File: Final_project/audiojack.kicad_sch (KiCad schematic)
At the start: 15 parts

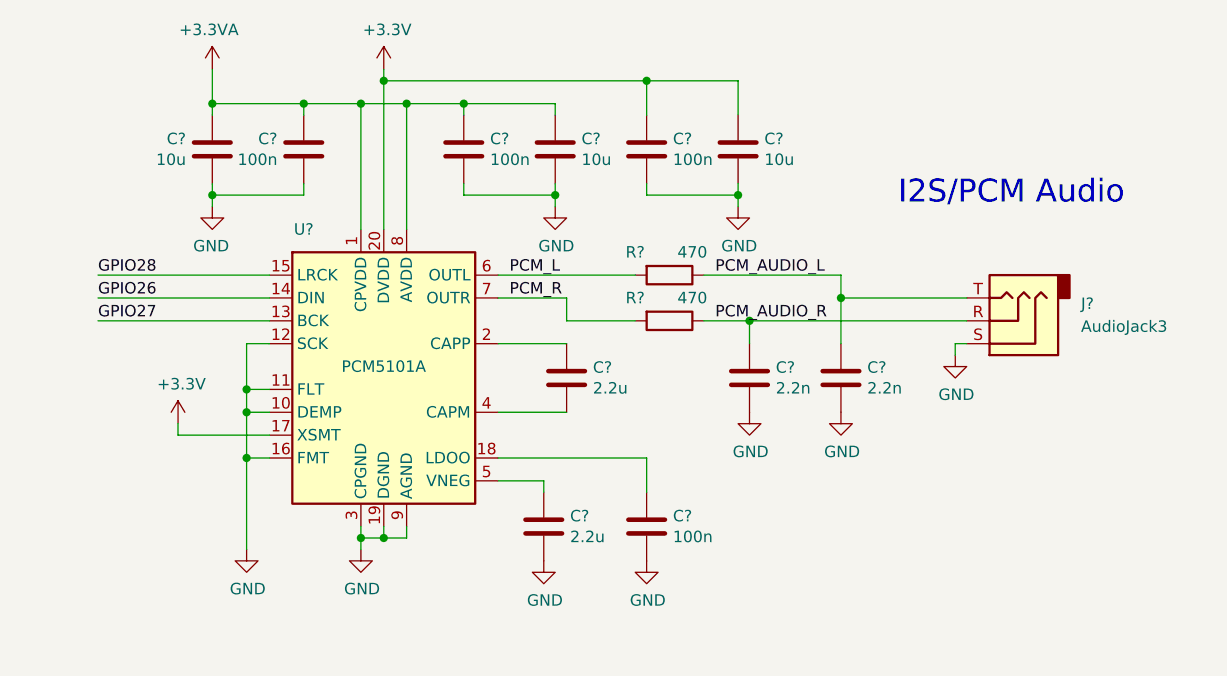
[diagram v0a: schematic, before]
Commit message: assigned footprints to audiojack caps
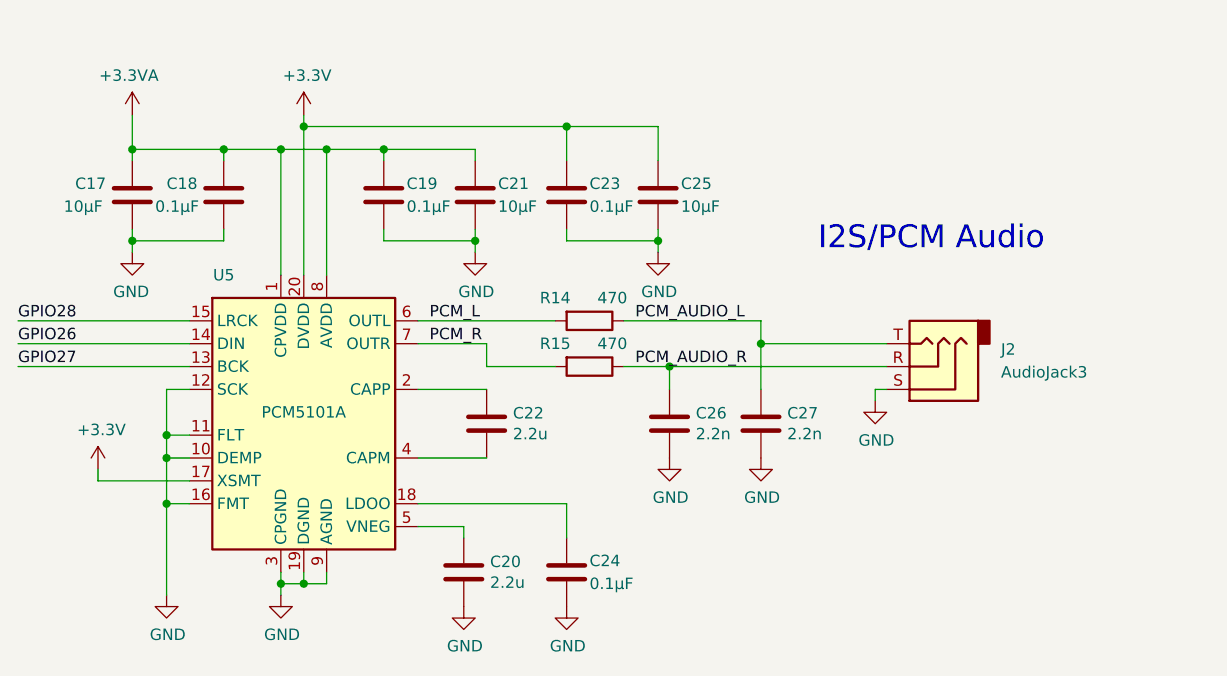
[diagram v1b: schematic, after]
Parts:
- removed C? (x3): 10u, Capacitor_SMD:C_0603_1608Metric, symbol Device:C
- removed C? (x2): 2.2n, Capacitor_SMD:C_0402_1005Metric, symbol Device:C
- removed C? (x4): 100n, Capacitor_SMD:C_0402_1005Metric, symbol Device:C
- removed C? (x2): 2.2u, Capacitor_SMD:C_0603_1608Metric, symbol Device:C
- removed J?: AudioJack3, symbol Connector:AudioJack3
- removed R? (x2): 470, Resistor_SMD:R_0402_1005Metric, symbol Device:R
- removed U?: PCM5101A, Package_SO:TSSOP-20_4.4x6.5mm_P0.65mm, symbol Audio:PCM5101
- added C17, C21, C25: 10µF, Final_project:GRM188R61E106KA73D, symbol Device:C
- added C18, C19, C23, C24: 0.1µF, Final_project:CL10B104JB8NNNC, symbol Device:C
- added C20, C22: 2.2u, Capacitor_SMD:C_0603_1608Metric, symbol Device:C
- added C26, C27: 2.2n, Capacitor_SMD:C_0402_1005Metric, symbol Device:C
- added J2: AudioJack3, Connector_Audio:Jack_3.5mm_Lumberg_1503_07_Horizontal, symbol Connector:AudioJack3
- added R14, R15: 470, Resistor_SMD:R_0402_1005Metric, symbol Device:R
- added U5: PCM5101A, Package_SO:TSSOP-20_4.4x6.5mm_P0.65mm, symbol Audio:PCM5101
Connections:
- net +3.3V: now also C23.2, C25.1, U5.17 (XSMT), U5.20 (DVDD)
- net +3.3VA: now also C17.1, C18.2, C19.2, C21.1, U5.1 (CPVDD), U5.8 (AVDD)
- net GND: now also C17.2, C18.1, C19.1, C20.2, C21.2, C23.1, C24.1, C25.2, C26.2, C27.2, J2.S, U5.10 (DEMP), U5.11 (FLT), U5.12 (SCK), U5.16 (FMT), U5.19 (DGND), U5.3 (CPGND), U5.9 (AGND)
- net GPIO26: now also U5.14 (DIN)
- net GPIO27: now also U5.13 (BCK)
- net GPIO28: now also U5.15 (LRCK)
- net PCM_AUDIO_L: now also C27.1, J2.T, R14.1
- net PCM_AUDIO_R: now also C26.1, J2.R, R15.1
- net PCM_L: now also R14.2, U5.6 (OUTL)
- net PCM_R: now also R15.2, U5.7 (OUTR)
- new net: C24.2, U5.18 (LDOO)
- new net: C22.1, U5.2 (CAPP)
- new net: C22.2, U5.4 (CAPM)
- new net: C20.1, U5.5 (VNEG)
